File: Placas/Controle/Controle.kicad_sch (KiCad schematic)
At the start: 0 parts

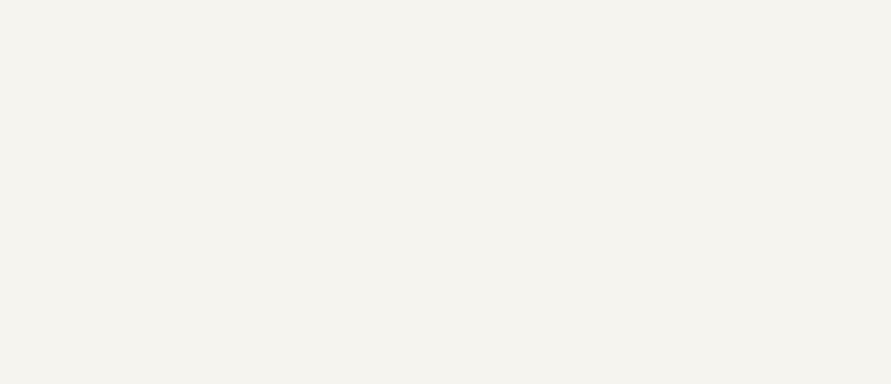
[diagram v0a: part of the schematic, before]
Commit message: Modificações nas duas placas, adição de furos para montagem, melhora na posição dos micros e conectores para comunicação SPI
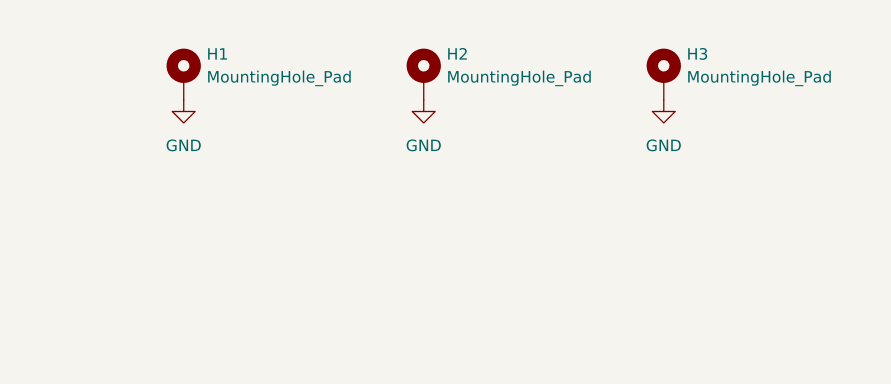
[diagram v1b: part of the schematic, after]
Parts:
- added H1, H2, H3: MountingHole_Pad, MountingHole:MountingHole_3.2mm_M3_Pad_Via, symbol Mechanical:MountingHole_Pad
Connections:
- new net GND: H1.1, H2.1, H3.1

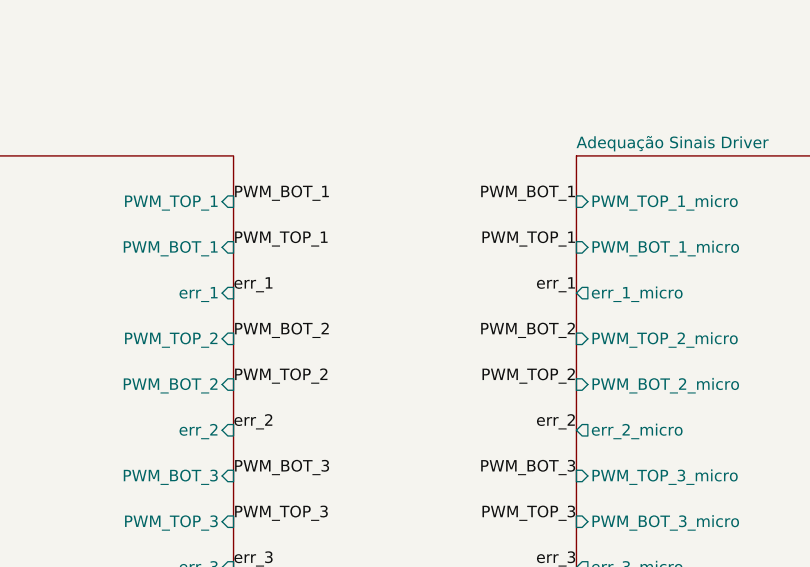
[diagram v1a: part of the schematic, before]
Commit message: Criação dos arquivos em C para o firmware dos dois micros e script em python para salvar aquisição dos dados e envio de comandos
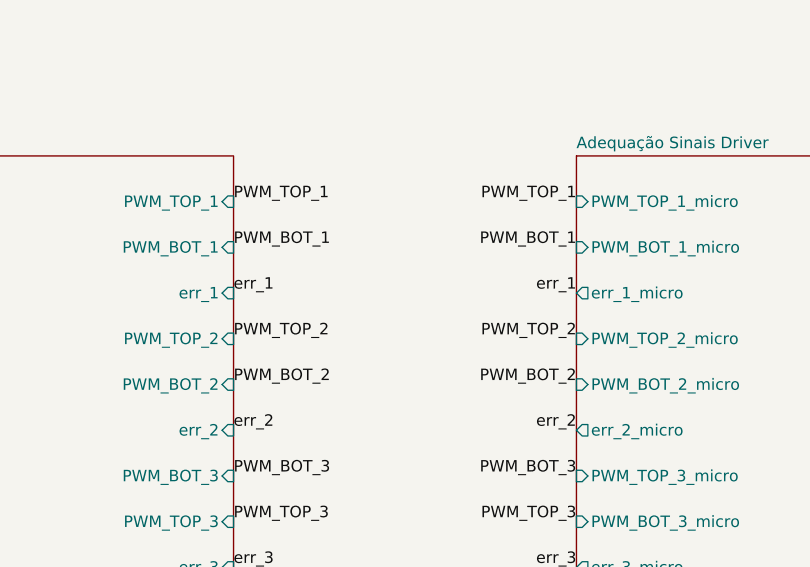
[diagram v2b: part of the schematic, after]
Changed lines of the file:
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@@
 	)
 	(label "PWM_TOP_1"
-		(at 210.82 109.22 180)
-		(effects
-			(font
-				(size 1.27 1.27)
-			)
-			(justify right bottom)
-		)
-	)
-	(label "PWM_TOP_2"
+		(at 210.82 104.14 180)
+		(effects
+			(font
+				(size 1.27 1.27)
+			)
+			(justify right bottom)
+		)
+	)
+	(label "PWM_BOT_2"
 		(at 172.72 124.46 0)
+		(effects
+			(font
+				(size 1.27 1.27)
+			)
+			(justify left bottom)
+		)
+	)
+	(label "PWM_BOT_1"
+		(at 172.72 109.22 0)
 		(effects
 			(font
@@
 		)
 	)
-	(label "PWM_BOT_1"
-		(at 210.82 104.14 180)
-		(effects
-			(font
-				(size 1.27 1.27)
-			)
-			(justify right bottom)
-		)
-	)
 	(label "I_read_out"
 		(at 74.93 140.97 0)
@@
 		)
 	)
-	(label "PWM_BOT_1"
-		(at 172.72 104.14 0)
-		(effects
-			(font
-				(size 1.27 1.27)
-			)
-			(justify left bottom)
+	(label "PWM_TOP_2"
+		(at 210.82 119.38 180)
+		(effects
+			(font
+				(size 1.27 1.27)
+			)
+			(justify right bottom)
 		)
 	)
@@
 		)
 	)
+	(label "PWM_TOP_1"
+		(at 172.72 104.14 0)
+		(effects
+			(font
+				(size 1.27 1.27)
+			)
+			(justify left bottom)
+		)
+	)
+	(label "PWM_BOT_2"
+		(at 210.82 124.46 180)
+		(effects
+			(font
+				(size 1.27 1.27)
+			)
+			(justify right bottom)
+		)
+	)
 	(label "V_read_out"
 		(at 74.93 115.57 0)
@@
 		)
 	)
-	(label "PWM_BOT_2"
-		(at 172.72 119.38 0)
-		(effects
-			(font
-				(size 1.27 1.27)
-			)
-			(justify left bottom)
-		)
-	)
 	(label "I_read_L3"
 		(at 109.22 134.62 180)
@@
 		)
 	)
-	(label "PWM_TOP_1"
-		(at 172.72 109.22 0)
-		(effects
-			(font
-				(size 1.27 1.27)
-			)
-			(justify left bottom)
+	(label "PWM_BOT_1"
+		(at 210.82 109.22 180)
+		(effects
+			(font
+				(size 1.27 1.27)
+			)
+			(justify right bottom)
 		)
 	)
@@
 		)
 	)
-	(label "PWM_BOT_2"
-		(at 210.82 119.38 180)
-		(effects
-			(font
-				(size 1.27 1.27)
-			)
-			(justify right bottom)
-		)
-	)
 	(label "V_read_in"
 		(at 109.22 109.22 180)
@@
 		)
 	)
+	(label "PWM_TOP_2"
+		(at 172.72 119.38 0)
+		(effects
+			(font
+				(size 1.27 1.27)
+			)
+			(justify left bottom)
+		)
+	)
 	(label "I_read_L2"
 		(at 109.22 128.27 180)
 		(effects
 			(font
-				(size 1.27 1.27)
-			)
-			(justify right bottom)
-		)
-	)
-	(label "PWM_TOP_2"
-		(at 210.82 124.46 180)
-		(effects
-			(font
